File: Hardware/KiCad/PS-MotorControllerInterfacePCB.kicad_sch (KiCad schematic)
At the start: 42 parts, among them J1 PWR board, J2 CAN board out, J3 CAN board in, J4 Candapter, J5 53307-2471, J6 CAN board -> mppt +moco, J7 CAN mppts + moco -> board, J8 PWR Moco

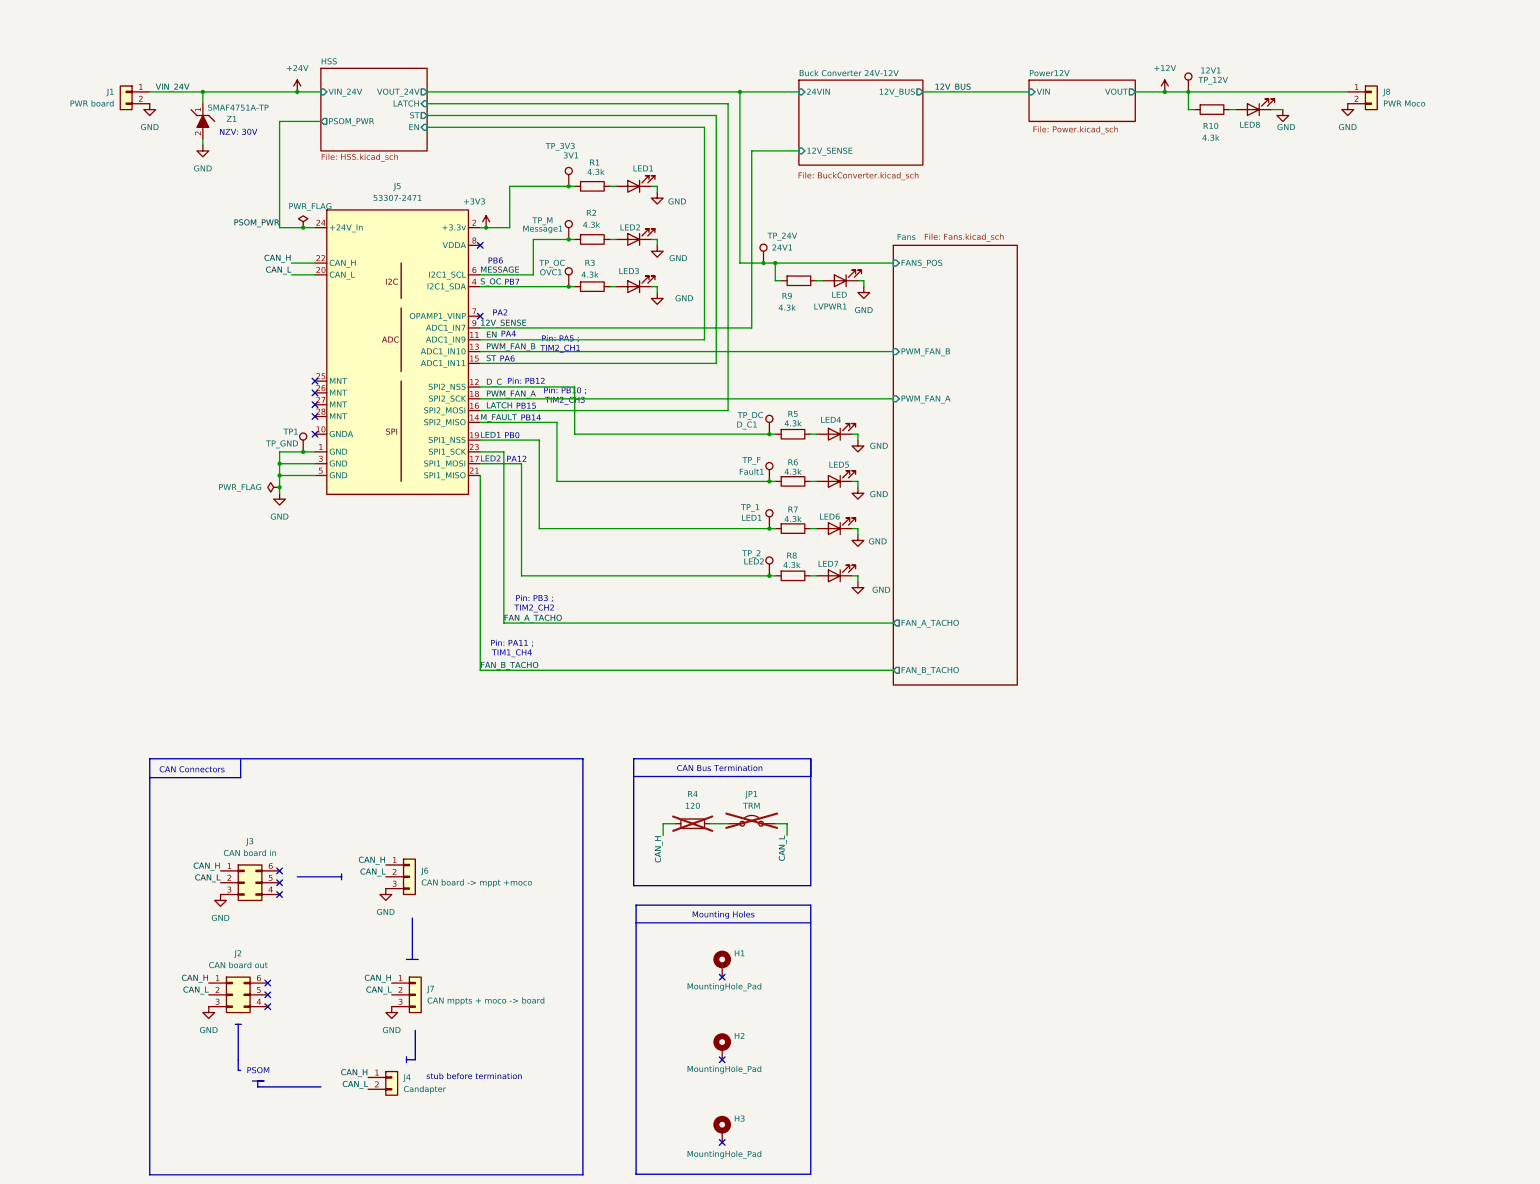
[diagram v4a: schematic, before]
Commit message: layout ready for review
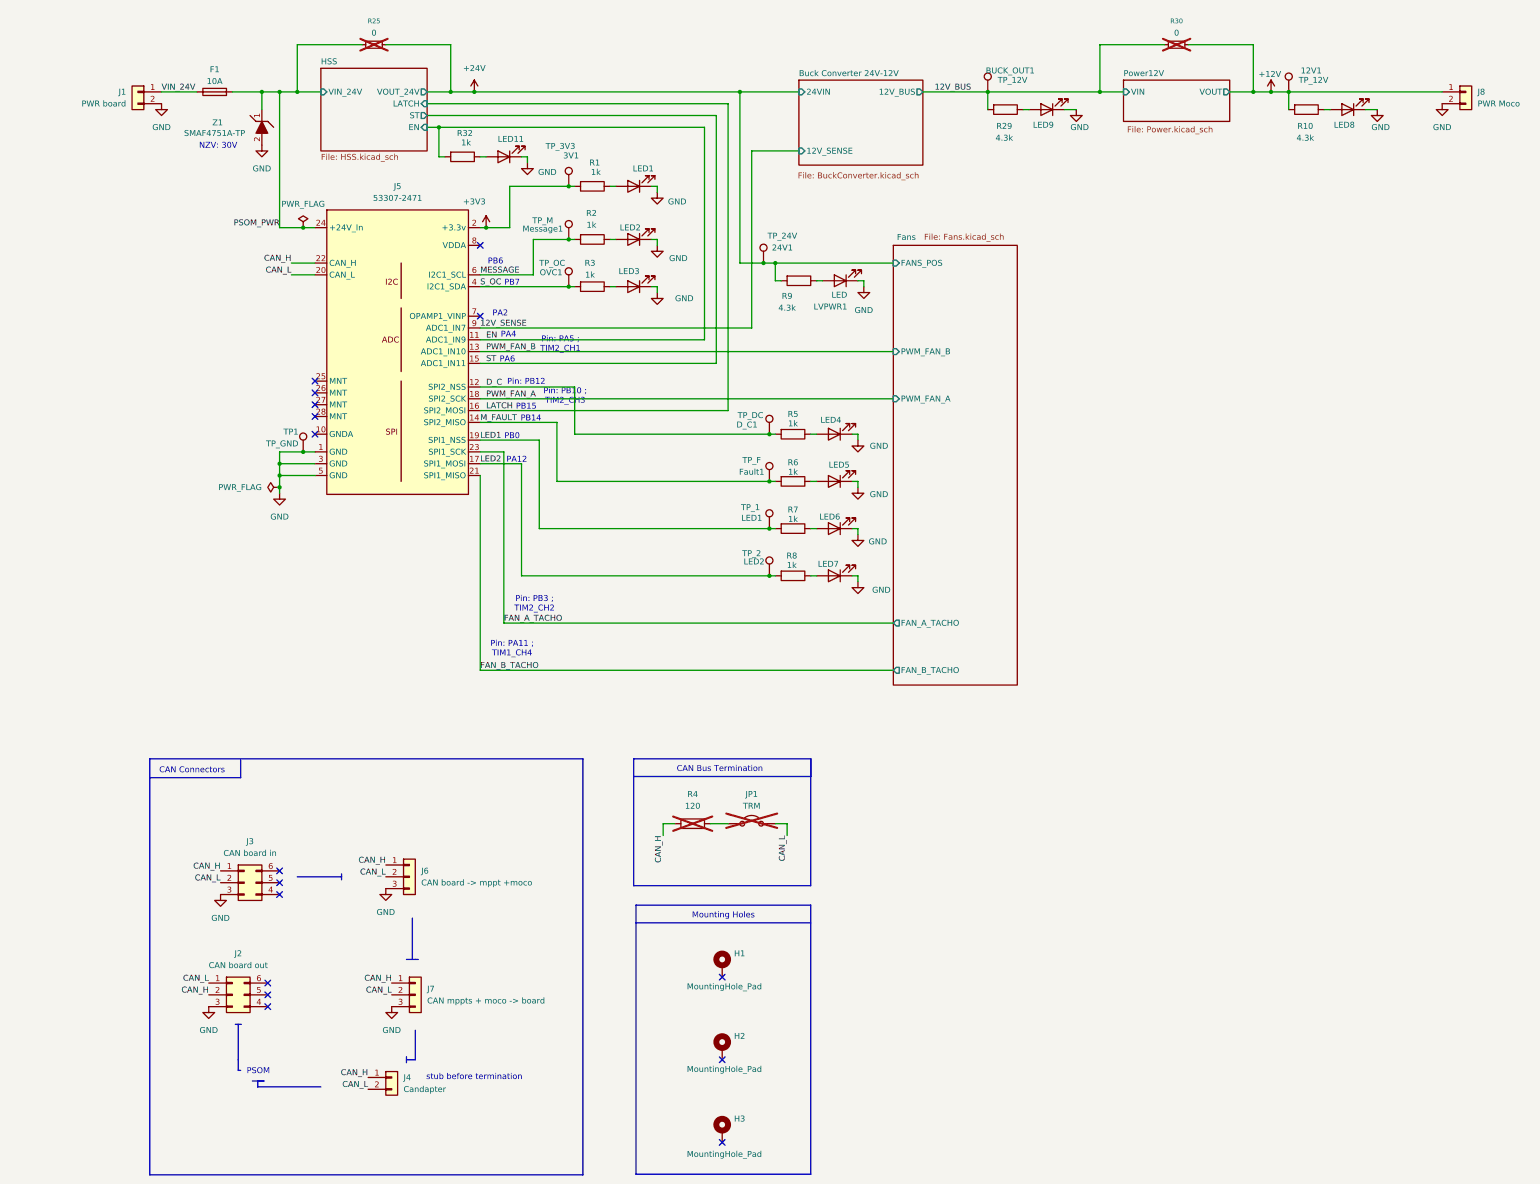
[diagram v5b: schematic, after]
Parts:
- added BUCK_OUT1: TP_12V, TestPoint:TestPoint_Pad_1.0x1.0mm, symbol Connector:TestPoint
- added F1: 10A, Moco:FUSE_3568, symbol Device:Fuse
- added LED11, LED9: LED, LED_SMD:LED_0603_1608Metric, symbol Device:LED
- added R25, R30: 0, Resistor_SMD:R_0603_1608Metric_Pad0.98x0.95mm_HandSolder, symbol Device:R_Small
- added R29: 4.3k, Resistor_SMD:R_0603_1608Metric_Pad0.98x0.95mm_HandSolder, symbol Device:R
- added R32: 1k, Resistor_SMD:R_0603_1608Metric_Pad0.98x0.95mm_HandSolder, symbol Device:R
- R1, R2, R3, R5, R6, R7, R8: value 4.3k -> 1k
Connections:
- net Buck Converter 24V-12V/24VIN is gone; now on net +24V: 24V1.1, R9.2
- net +12V: now also R30.2
- net +24V: now also R25.2; no longer J1.1 (Pin_1), Z1.1 (K)
- net 12V_BUS: now also BUCK_OUT1.1, R29.2, R30.1
- net CAN_H: now also J2.2 (Pin_2); no longer J2.1 (Pin_1)
- net CAN_L: now also J2.1 (Pin_1); no longer J2.2 (Pin_2)
- net EN: now also R32.2
- net GND: now also LED11.1 (K), LED9.1 (K)
- net PSOM_PWR: now also Z1.1 (K), F1.2, R25.1
- new net: LED9.2 (A), R29.1
- new net: LED11.2 (A), R32.1
- new net VIN_24V: F1.1, J1.1 (Pin_1)
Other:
- sheet HSS ports: added none; removed PSOM_PWR
- moved on the sheet: 12V1, J1, J8, LED8, R10, Z1

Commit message: changes
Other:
- moved on the sheet: 3V1, D_C1, Fault1, LED1, LED2, LED3, LED4, LED5, LED6, LED7, Message1, OVC1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

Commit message: layout done
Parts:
- removed F1: 10A, Moco:FUSE_3568, symbol Device:Fuse
- added F1: Fuse_3568, UTSVT_Connectors:FUSE_3568, symbol UTSVT_Powers:Fuse_3568
- added TP2: 12V_Sense, TestPoint:TestPoint_Pin_1.0x1.0mm, symbol Connector:TestPoint
- added TP5: TP_EN, TestPoint:TestPoint_Pin_1.0x1.0mm, symbol Connector:TestPoint
- 12V1, 24V1, 3V1, BUCK_OUT1, Message1, OVC1, TP1, TP_1, TP_2: footprint TestPoint:TestPoint_Pad_1.0x1.0mm -> TestPoint:TestPoint_Pin_1.0x1.0mm
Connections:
- net 12V_SENSE: now also TP2.1
- net EN: now also TP5.1
- net PSOM_PWR: now also F1.2
- net VIN_24V: now also F1.1

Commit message: done with changes
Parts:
- removed H3: MountingHole_Pad, MountingHole:MountingHole_3.2mm_M3_Pad_TopBottom, symbol Mechanical:MountingHole_Pad
- added R34: 0, Resistor_SMD:R_0603_1608Metric_Pad0.98x0.95mm_HandSolder, symbol Device:R
- 12VSNS1: renamed from TP2; footprint TestPoint:TestPoint_Pin_1.0x1.0mm -> TestPoint:TestPoint_Keystone_5000-5004_Miniature; now in the parts list
- 24V1, BUCK_OUT1, TP1, TP_1, TP_2: footprint TestPoint:TestPoint_Pin_1.0x1.0mm -> TestPoint:TestPoint_Keystone_5000-5004_Miniature; now in the parts list
- 3V3: renamed from 3V1; value TP_3V3 -> 3V3; footprint TestPoint:TestPoint_Pin_1.0x1.0mm -> TestPoint:TestPoint_Keystone_5000-5004_Miniature; now in the parts list
- FAULT1: renamed from Fault1; footprint TestPoint:TestPoint_Pad_1.0x1.0mm -> TestPoint:TestPoint_Keystone_5000-5004_Miniature; now in the parts list
- HSS_EN1: renamed from TP5; footprint TestPoint:TestPoint_Pin_1.0x1.0mm -> TestPoint:TestPoint_Keystone_5000-5004_Miniature; now in the parts list
- I_MOTOR1: renamed from D_C1; footprint TestPoint:TestPoint_Pad_1.0x1.0mm -> TestPoint:TestPoint_Keystone_5000-5004_Miniature; now in the parts list
- PP_OUT1: renamed from 12V1; footprint TestPoint:TestPoint_Pin_1.0x1.0mm -> TestPoint:TestPoint_Keystone_5000-5004_Miniature; now in the parts list
- STATUS1: renamed from Message1; footprint TestPoint:TestPoint_Pin_1.0x1.0mm -> TestPoint:TestPoint_Keystone_5000-5004_Miniature; now in the parts list
- SW_OC1: renamed from OVC1; footprint TestPoint:TestPoint_Pin_1.0x1.0mm -> TestPoint:TestPoint_Keystone_5000-5004_Miniature; now in the parts list
- renumbered J6 to CAN(board->moco,mppts)1, J7 to CAN(moco,mppts->board)1, J4 to CANDAPTER1, J3 to CAN_IN1, J2 to CAN_OUT1, J8 to PWR_12V1, J1 to PWR_BOARD1
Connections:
- net GND: now also R34.2; no longer CAN(board->moco,mppts)1.3 (Pin_3), CAN(moco,mppts->board)1.3 (Pin_3), CAN_IN1.3 (Pin_3), CAN_OUT1.3 (Pin_3)
- net D_C renamed I_MOTOR
- net EN renamed HSS_EN
- net MESSAGE renamed STATUS
- net M_FAULT renamed FAULT
- net PWM_FAN_A renamed PWM_A
- net PWM_FAN_B renamed PWM_B
- net ST renamed HSS_FAULT
- net S_OC renamed SW_OC
- new net SHIELD: CAN_IN1.3 (Pin_3), CAN_OUT1.3 (Pin_3), R34.1
- no-connect marks 16 -> 17
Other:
- note added: "10A"
